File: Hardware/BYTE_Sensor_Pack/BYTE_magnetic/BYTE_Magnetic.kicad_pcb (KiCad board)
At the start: 2 copper layers, 18 x 23 mm, 20 parts, among them J1 Input, M1 Motor_DC, U1 DRV2605LDGS, U2 ADS1115IDGS, U3 PTCA9536BDTMR, U4 SI7210-B-12-IM2, U5 SI7210-B-13-IM2, U6 SI7210-B-14-IM2

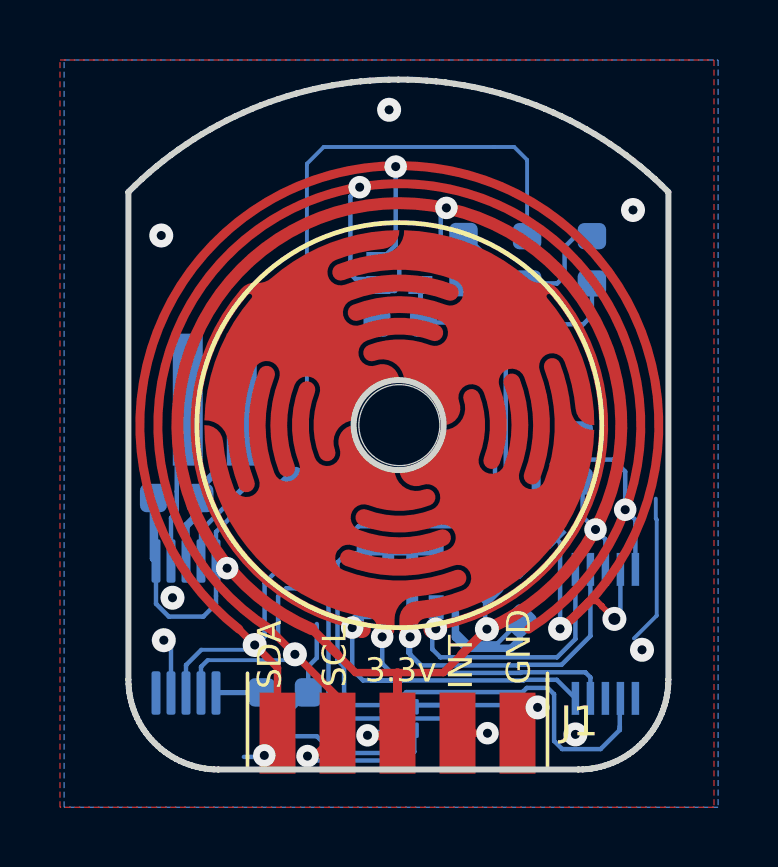
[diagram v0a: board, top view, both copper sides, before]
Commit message: move ICs 0.5 to center, magnetic sensor
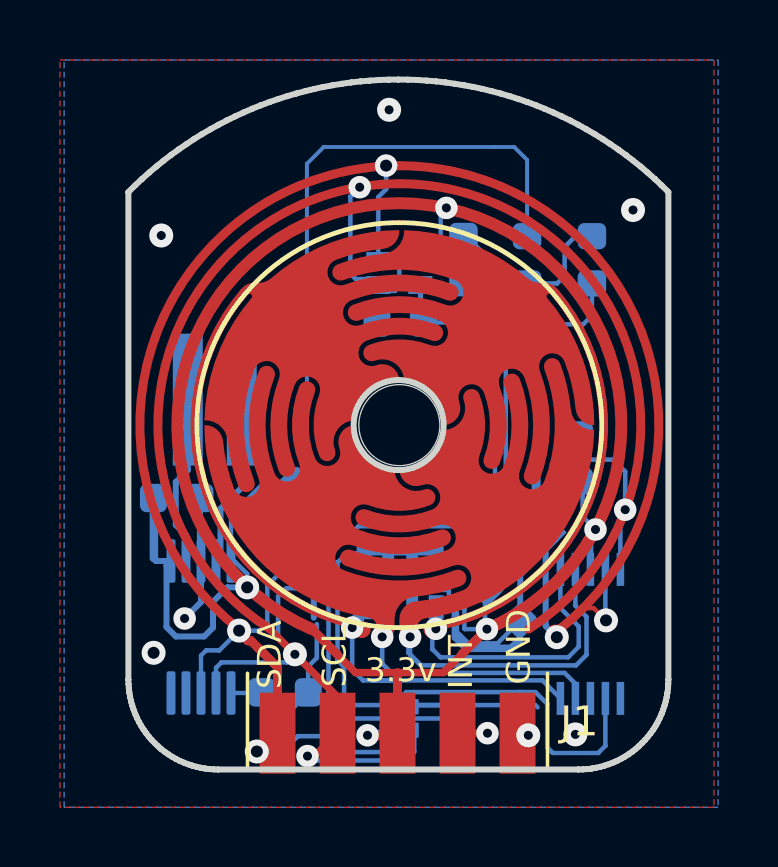
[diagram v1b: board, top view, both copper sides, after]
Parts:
- moved U1 0.50 mm to (175.4, 118.4)
- moved U2 0.50 mm to (188.4, 118.6)
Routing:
- net +3V3: track 42.3 -> 49.3 mm
- net GND: track 37.7 -> 34.6 mm, vias 8 -> 7
- net Net-(M1-Pad1): track 6.95 -> 9.19 mm
- net Net-(C4-Pad1): track 2.79 -> 1.03 mm
- net /A2: track 9.12 -> 10.4 mm
- net /SCL: track 31.5 -> 30.2 mm
- net /A0: track 11.5 -> 10.9 mm
- net /A1: track 12.2 -> 11.7 mm

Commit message: prepare for manufacture
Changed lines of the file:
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@@
   (general
     (thickness 0.8)
-    (drawings 140)
+    (drawings 141)
     (tracks 366)
     (zones 0)
@@
       (drillshape 0)
       (scaleselection 1)
-      (outputdirectory "./"))
+      (outputdirectory "magneticSensorV1.0Gerbers/"))
   )
   (net 0 "")
@@
       (effects (font (size 0.8 0.8) (thickness 0.12)))
     )
-    (pad "#" np_thru_hole circle (at 0 0) (size 2.7 2.7) (drill 2.7) (layers *.Cu *.Mask))
     (pad 5 smd custom (at 5.346 6.8) (size 0.2 0.2) (layers F.Cu)
       (net 4 /SDA) (zone_connect 0)
@@
            (xy -0.093 -0.118)) (width 0))
       ))
-    (pad 1 smd custom (at -1.25 6.8) (size 0.2 0.2) (layers F.Cu F.Mask)
+    (pad 1 smd custom (at -1.25 6.8) (size 0.2 0.2) (layers F.Cu)
       (net 13 /A1) (zone_connect 0)
       (options (clearance outline) (anchor circle))
@@
            (xy 2.428 -9.6) (xy 2.332 -9.619)) (width 0))
       ))
-    (pad 2 smd custom (at 1.1 6.8) (size 0.2 0.2) (layers F.Cu F.Mask)
+    (pad 2 smd custom (at 1.1 6.8) (size 0.2 0.2) (layers F.Cu)
       (net 14 /A2) (zone_connect 0)
       (options (clearance outline) (anchor circle))
@@
            (xy 3.192 -5.589) (xy 3.063 -5.202)) (width 0))
       ))
-    (pad 3 smd custom (at -0.46 6.8) (size 0.2 0.2) (layers F.Cu F.Mask)
+    (pad 3 smd custom (at -0.46 6.8) (size 0.2 0.2) (layers F.Cu)
       (net 12 /A0) (zone_connect 0)
       (options (clearance outline) (anchor circle))
@@
            (xy -2.555 -6.958) (xy -2.522 -7.272) (xy -2.456 -7.581) (xy -2.358 -7.882)) (width 0))
       ))
-    (pad 4 smd custom (at 0.3 6.8) (size 0.2 0.2) (layers F.Cu F.Mask)
+    (pad 4 smd custom (at 0.3 6.8) (size 0.2 0.2) (layers F.Cu)
       (net 15 /A3) (zone_connect 0)
       (options (clearance outline) (anchor circle))
@@
     )
   )
+  (gr_circle (center 182.01 111.67) (end 185.53 111.5) (layer F.Mask) (width 6))
   (gr_text SDA (at 177.69 119.32 90) (layer F.SilkS)
     (effects (font (size 0.8 0.8) (thickness 0.12)))
@@
     (effects (font (size 0.8 0.8) (thickness 0.12)))
   )
-  (via (at 181.57 103.02) (size 0.75) (drill 0.4) (layers F.Cu B.Cu) (net 4))
   (segment (start 178.849239 115.600711) (end 178.578539 115.330011) (width 0.15) (layer B.Cu) (net 1))
   (segment (start 178.578539 115.330011) (end 178.306443 115.330011) (width 0.15) (layer B.Cu) (net 1))
@@
   (segment (start 176.08 119.58) (end 178.26 119.58) (width 0.15) (layer B.Cu) (net 3))
   (segment (start 178.26 119.58) (end 178.53 119.31) (width 0.15) (layer B.Cu) (net 3))
+  (via (at 181.57 103.02) (size 0.75) (drill 0.4) (layers F.Cu B.Cu) (net 4))
   (segment (start 187.239239 115.459289) (end 186.89 115.808528) (width 0.2) (layer B.Cu) (net 4))
   (via (at 187.26 118.74) (size 0.8) (drill 0.4) (layers F.Cu B.Cu) (net 4))
